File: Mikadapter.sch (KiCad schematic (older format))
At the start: 7 parts, among them J1 RJ45, J2 Conn_01x03_Female, J3 RJ45, J4 Conn_01x03_Female, J5 Conn_01x02_Female, J6 Conn_01x03_Female, J7 Conn_01x02_Female

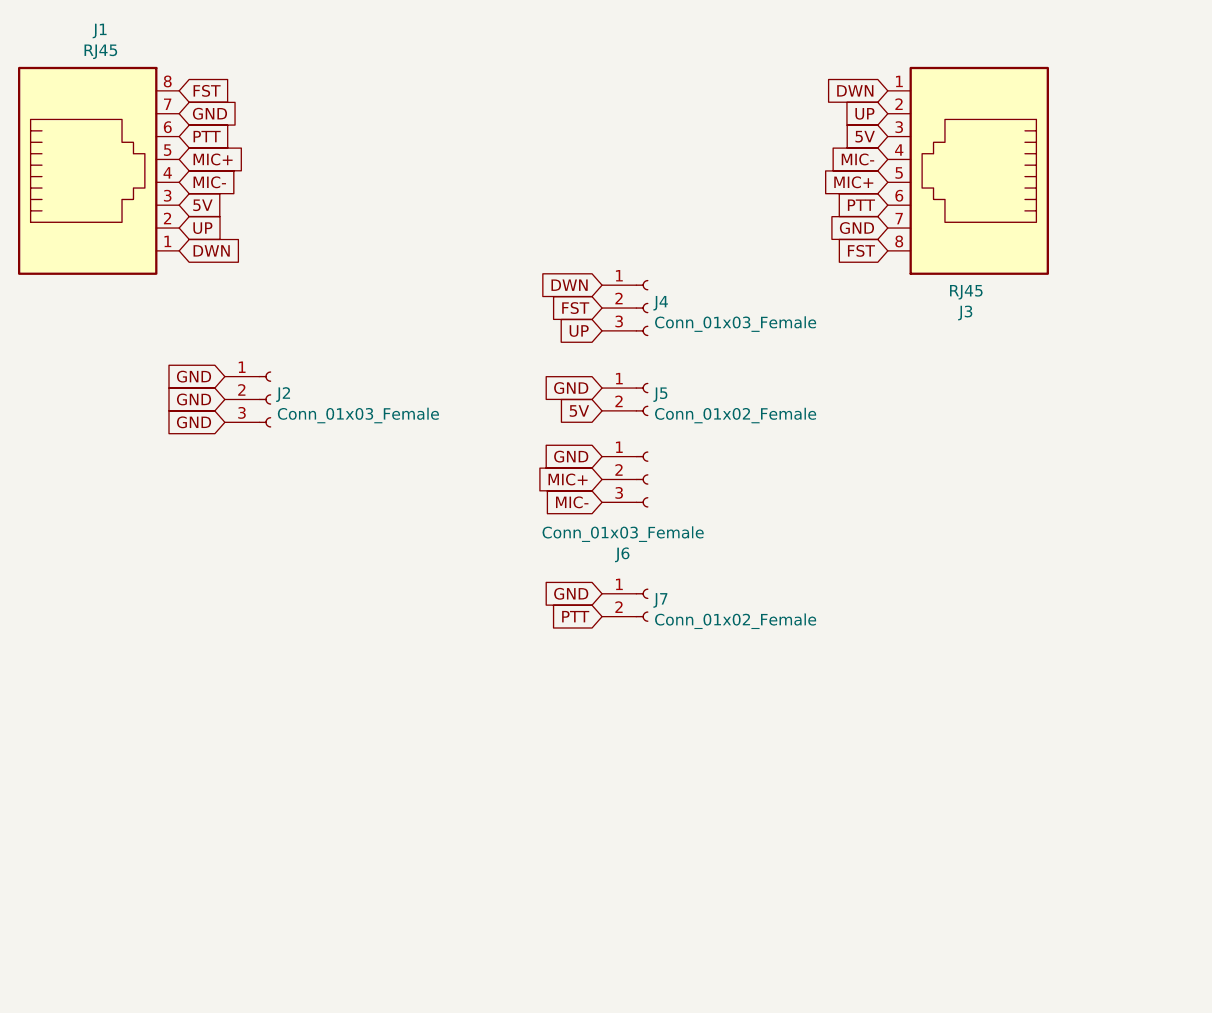
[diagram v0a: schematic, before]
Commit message: changed layout for FST|DWN|UP buttons
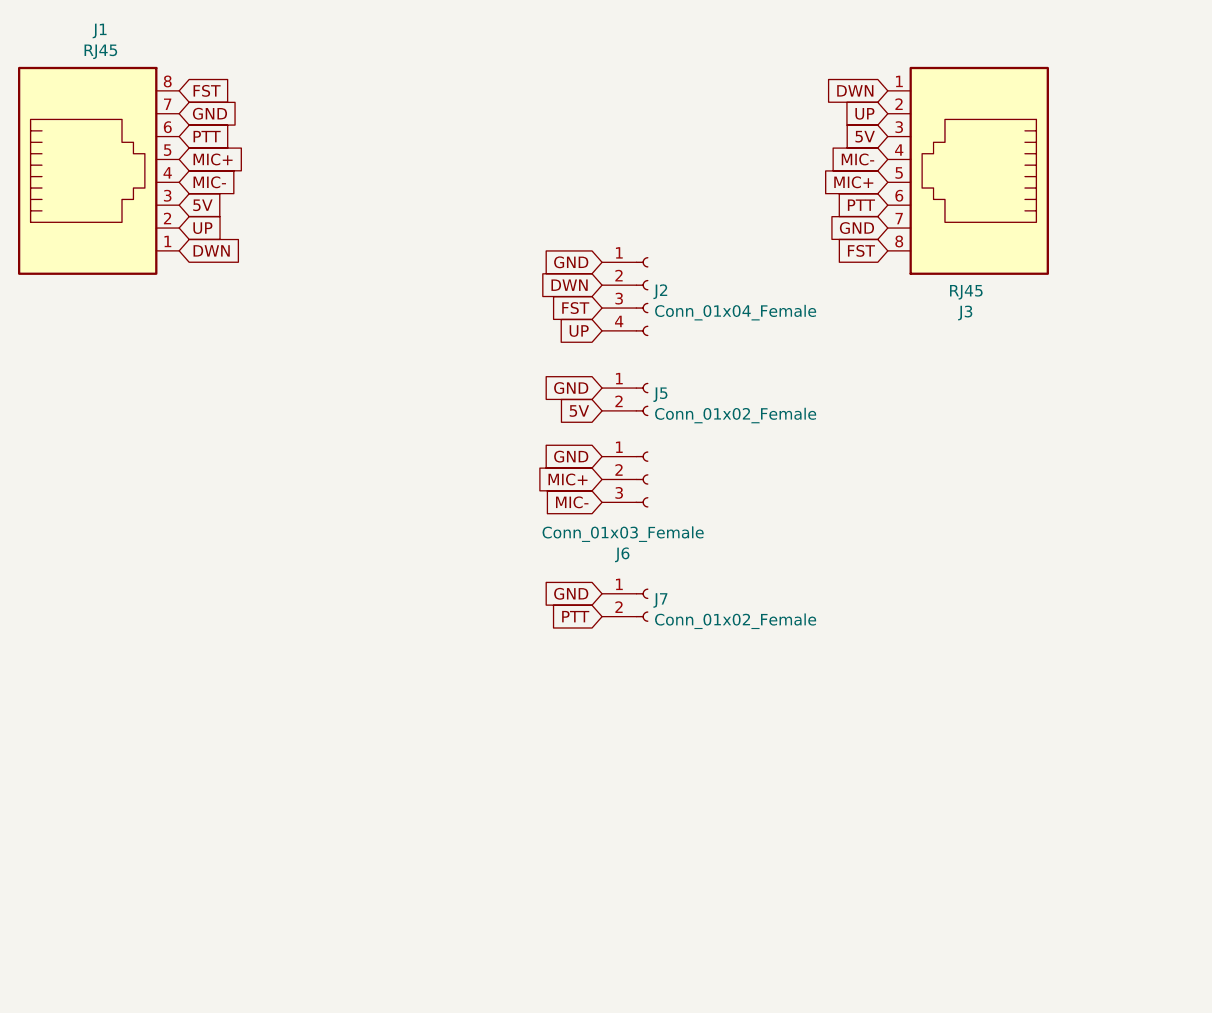
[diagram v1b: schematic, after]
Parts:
- removed J2, J4: Conn_01x03_Female, Connector_PinHeader_2.54mm:PinHeader_1x03_P2.54mm_Vertical, symbol Connector:Conn_01x03_Female
- added J2: Conn_01x04_Female, Connector_PinHeader_2.54mm:PinHeader_1x04_P2.54mm_Vertical, symbol Connector:Conn_01x04_Female
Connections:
- net DWN: now also J2.2 (Pin_2)
- net FST: now also J2.3 (Pin_3)
- net GND: now also J2.1 (Pin_1)
- net UP: now also J2.4 (Pin_4)
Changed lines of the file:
@@
 Text GLabel 5250 3700 0    50   Input ~ 0
 5V
-$Comp
-L Connector:Conn_01x03_Female J4
-U 1 1 607373F2
-P 5450 3250
-F 0 "J4" H 5478 3276 50  0000 L CNN
-F 1 "Conn_01x03_Female" H 5478 3185 50  0000 L CNN
-F 2 "Connector_PinHeader_2.54mm:PinHeader_1x03_P2.54mm_Vertical" H 5450 3250 50  0001 C CNN
-F 3 "~" H 5450 3250 50  0001 C CNN
-	1    5450 3250
-	1    0    0    -1
-$EndComp
-$Comp
-L Connector:Conn_01x03_Female J2
-U 1 1 60738991
-P 3800 3650
-F 0 "J2" H 3828 3676 50  0000 L CNN
-F 1 "Conn_01x03_Female" H 3828 3585 50  0000 L CNN
-F 2 "Connector_PinHeader_2.54mm:PinHeader_1x03_P2.54mm_Vertical" H 3800 3650 50  0001 C CNN
-F 3 "~" H 3800 3650 50  0001 C CNN
-	1    3800 3650
-	1    0    0    -1
-$EndComp
-Text GLabel 3600 3550 0    50   Input ~ 0
-GND
-Text GLabel 3600 3650 0    50   Input ~ 0
-GND
-Text GLabel 3600 3750 0    50   Input ~ 0
+Text GLabel 5250 3050 0    50   Input ~ 0
 GND
 Text GLabel 5250 3150 0    50   Input ~ 0
@@
 Text GLabel 5250 3250 0    50   Input ~ 0
 FST
+$Comp
+L Connector:Conn_01x04_Female J2
+U 1 1 6077AEAE
+P 5450 3150
+F 0 "J2" H 5478 3126 50  0000 L CNN
+F 1 "Conn_01x04_Female" H 5478 3035 50  0000 L CNN
+F 2 "Connector_PinHeader_2.54mm:PinHeader_1x04_P2.54mm_Vertical" H 5450 3150 50  0001 C CNN
+F 3 "~" H 5450 3150 50  0001 C CNN
+	1    5450 3150
+	1    0    0    -1
+$EndComp
 $EndSCHEMATC

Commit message: transformed in KiCAD 6 and changed layout and changed pinout for RJ45
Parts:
- added J1, J3, J4: FC68131, Addtional_DO7GN:CLIFF_FC68131, symbol FC68131:FC68131
- added J9: Conn_01x03_Female, Connector_PinHeader_2.54mm:PinHeader_1x02_P2.54mm_Vertical, symbol Connector:Conn_01x02_Female
- J6: footprint Connector_PinHeader_2.54mm:PinHeader_1x03_P2.54mm_Vertical -> Connector_PinHeader_2.54mm:PinHeader_1x02_P2.54mm_Vertical; symbol Connector:Conn_01x03_Female -> Connector:Conn_01x02_Female
- RJ45OUT1: renamed from J3; value RJ45 -> RJ45OUT
- renumbered J1 to RJ45IN1
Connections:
- net 5V: now also RJ45IN1.6, RJ45OUT1.6; no longer RJ45IN1.3, RJ45OUT1.3
- net DWN: now also RJ45IN1.8, RJ45OUT1.8; no longer RJ45IN1.1, RJ45OUT1.1
- net FST: now also RJ45IN1.1, RJ45OUT1.1; no longer RJ45IN1.8, RJ45OUT1.8
- net GND: now also RJ45IN1.2, RJ45OUT1.2; no longer J6.1 (Pin_1), RJ45IN1.7, RJ45OUT1.7
- net MIC+: now also RJ45IN1.4, RJ45OUT1.4, J1.2; no longer RJ45IN1.5, RJ45OUT1.5
- net MIC-: now also J6.1 (Pin_1), RJ45IN1.5, RJ45OUT1.5, J1.1; no longer J6.3 (Pin_3), RJ45IN1.4, RJ45OUT1.4
- net PTT: now also RJ45IN1.3, RJ45OUT1.3; no longer RJ45IN1.6, RJ45OUT1.6
- net UP: now also RJ45IN1.7, RJ45OUT1.7; no longer RJ45IN1.2, RJ45OUT1.2
- new net Audio+: J3.2, J4.2, J9.2 (Pin_2)
- new net Audio-: J3.1, J4.1, J9.1 (Pin_1)
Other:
- moved on the sheet: RJ45OUT1
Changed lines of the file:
@@
 $EndDescr
 $Comp
-L Connector:RJ45 J1
+L Connector:RJ45 RJ45IN1
 U 1 1 5EAEC084
 P 3000 2700
-F 0 "J1" H 3057 3367 50  0000 C CNN
+F 0 "RJ45IN1" H 3057 3367 50  0000 C CNN
 F 1 "RJ45" H 3057 3276 50  0000 C CNN
 F 2 "Connector_RJ:RJ45_Wuerth_7499010001A_Horizontal" V 3000 2725 50  0001 C CNN
@@
 	1    0    0    -1
 $EndComp
-Text GLabel 3400 3000 2    50   Input ~ 0
-DWN
-Text GLabel 3400 2900 2    50   Input ~ 0
-UP
-Text GLabel 3400 2500 2    50   Input ~ 0
-PTT
-Text GLabel 3400 2300 2    50   Input ~ 0
-FST
-Text GLabel 3400 2400 2    50   Input ~ 0
-GND
-Text GLabel 3400 2600 2    50   Input ~ 0
-MIC+
-Text GLabel 3400 2700 2    50   Input ~ 0
-MIC-
-Text GLabel 3400 2800 2    50   Input ~ 0
-5V
-$Comp
-L Connector:RJ45 J3
+Text GLabel 3950 2700 2    50   Input ~ 0
+UP
+Text GLabel 3950 2300 2    50   Input ~ 0
+PTT
+Text GLabel 3950 2200 2    50   Input ~ 0
+GND
+Text GLabel 3950 2600 2    50   Input ~ 0
+5V
+$Comp
+L Connector:RJ45 RJ45OUT1
 U 1 1 606F46DC
-P 6900 2600
-F 0 "J3" H 6957 3267 50  0000 C CNN
-F 1 "RJ45" H 6957 3176 50  0000 C CNN
-F 2 "Connector_RJ:RJ45_Wuerth_7499010001A_Horizontal" V 6900 2625 50  0001 C CNN
-F 3 "~" V 6900 2625 50  0001 C CNN
-	1    6900 2600
-	-1   0    0    1
-$EndComp
-Text GLabel 6500 2300 0    50   Input ~ 0
-DWN
-Text GLabel 6500 2400 0    50   Input ~ 0
-UP
-Text GLabel 6500 2800 0    50   Input ~ 0
-PTT
-Text GLabel 6500 3000 0    50   Input ~ 0
-FST
-Text GLabel 6500 2900 0    50   Input ~ 0
-GND
-Text GLabel 6500 2700 0    50   Input ~ 0
-MIC+
-Text GLabel 6500 2600 0    50   Input ~ 0
-MIC-
-Text GLabel 6500 2500 0    50   Input ~ 0
-5V
+P 3000 3800
+F 0 "RJ45OUT1" H 3057 4467 50  0000 C CNN
+F 1 "RJ45OUT" H 3057 4376 50  0000 C CNN
+F 2 "Connector_RJ:RJ45_Wuerth_7499010001A_Horizontal" V 3000 3825 50  0001 C CNN
+F 3 "~" V 3000 3825 50  0001 C CNN
+	1    3000 3800
+	1    0    0    -1
+$EndComp
 $Comp
 L Connector:Conn_01x02_Female J7
@@
 Text GLabel 5250 4500 0    50   Input ~ 0
 GND
-$Comp
-L Connector:Conn_01x03_Female J6
-U 1 1 6071E719
-P 5450 4000
-F 0 "J6" H 5342 3675 50  0000 C CNN
-F 1 "Conn_01x03_Female" H 5342 3766 50  0000 C CNN
-F 2 "Connector_PinHeader_2.54mm:PinHeader_1x03_P2.54mm_Vertical" H 5450 4000 50  0001 C CNN
-F 3 "~" H 5450 4000 50  0001 C CNN
-	1    5450 4000
-	1    0    0    -1
-$EndComp
-Text GLabel 5250 4000 0    50   Input ~ 0
-MIC+
-Text GLabel 5250 4100 0    50   Input ~ 0
-MIC-
-Text GLabel 5250 3900 0    50   Input ~ 0
-GND
+Text GLabel 5400 4100 0    50   Input ~ 0
+MIC+
 $Comp
 L Connector:Conn_01x02_Female J5
@@
 	1    0    0    -1
 $EndComp
+Text GLabel 4550 6050 2    50   Input ~ 0
+Audio+
+Text GLabel 6750 5250 0    50   Input ~ 0
+Audio+
+Text GLabel 6750 5150 0    50   Input ~ 0
+Audio-
+$Comp
+L Connector:Conn_01x02_Female J9
+U 1 1 6079AC68
+P 6950 5150
+F 0 "J9" H 6978 5176 50  0000 L CNN
+F 1 "Conn_01x03_Female" H 6978 5085 50  0000 L CNN
+F 2 "Connector_PinHeader_2.54mm:PinHeader_1x02_P2.54mm_Vertical" H 6950 5150 50  0001 C CNN
+F 3 "~" H 6950 5150 50  0001 C CNN
+	1    6950 5150
+	1    0    0    -1
+$EndComp
+$Comp
+L Connector:Conn_01x02_Female J6
+U 1 1 6071E719
+P 5600 4000
+F 0 "J6" H 5492 3675 50  0000 C CNN
+F 1 "Conn_01x03_Female" H 5492 3766 50  0000 C CNN
+F 2 "Connector_PinHeader_2.54mm:PinHeader_1x02_P2.54mm_Vertical" H 5600 4000 50  0001 C CNN
+F 3 "~" H 5600 4000 50  0001 C CNN
+	1    5600 4000
+	1    0    0    -1
+$EndComp
+Text GLabel 3950 2400 2    50   Input ~ 0
+MIC+
+Text GLabel 3950 2100 2    50   Input ~ 0
+FST
+Text GLabel 3950 2800 2    50   Input ~ 0
+DWN
+Text GLabel 5550 6050 2    50   Input ~ 0
+Audio+
+Text GLabel 3650 6100 2    50   Input ~ 0
+MIC+
+Text GLabel 4550 5950 2    50   Input ~ 0
+Audio-
+Text GLabel 5550 5950 2    50   Input ~ 0
+Audio-
+Text GLabel 3650 6000 2    50   Input ~ 0
+MIC-
+Text GLabel 5400 4000 0    50   Input ~ 0
+MIC-
+Text GLabel 3950 2500 2    50   Input ~ 0
+MIC-
+$Comp
+L FC68131:FC68131 J1
+U 1 1 6156A03E
+P 3350 6000
+F 0 "J1" H 3394 6181 50  0000 C CNN
+F 1 "FC68131" H 3394 6090 50  0000 C CNN
+F 2 "Addtional_DO7GN:CLIFF_FC68131" H 3350 6000 50  0001 L BNN
+F 3 "" H 3350 6000 50  0001 L BNN
+F 4 "Manufacturer Recommendations" H 3350 6000 50  0001 L BNN "STANDARD"
+F 5 "Cliff" H 3350 6000 50  0001 L BNN "MANUFACTURER"
+F 6 "6.00 mm" H 3350 6000 50  0001 L BNN "MAXIMUM_PACKAGE_HEIGHT"
+F 7 "5" H 3350 6000 50  0001 L BNN "PARTREV"
+	1    3350 6000
+	1    0    0    -1
+$EndComp
+$Comp
+L FC68131:FC68131 J3
+U 1 1 61571E51
+P 4250 5950
+F 0 "J3" H 4294 6131 50  0000 C CNN
+F 1 "FC68131" H 4294 6040 50  0000 C CNN
+F 2 "Addtional_DO7GN:CLIFF_FC68131" H 4250 5950 50  0001 L BNN
+F 3 "" H 4250 5950 50  0001 L BNN
+F 4 "Manufacturer Recommendations" H 4250 5950 50  0001 L BNN "STANDARD"
+F 5 "Cliff" H 4250 5950 50  0001 L BNN "MANUFACTURER"
+F 6 "6.00 mm" H 4250 5950 50  0001 L BNN "MAXIMUM_PACKAGE_HEIGHT"
+F 7 "5" H 4250 5950 50  0001 L BNN "PARTREV"
+	1    4250 5950
+	1    0    0    -1
+$EndComp
+$Comp
+L FC68131:FC68131 J4
+U 1 1 615753B1
+P 5250 5950
+F 0 "J4" H 5294 6131 50  0000 C CNN
+F 1 "FC68131" H 5294 6040 50  0000 C CNN
+F 2 "Addtional_DO7GN:CLIFF_FC68131" H 5250 5950 50  0001 L BNN
+F 3 "" H 5250 5950 50  0001 L BNN
+F 4 "Manufacturer Recommendations" H 5250 5950 50  0001 L BNN "STANDARD"
+F 5 "Cliff" H 5250 5950 50  0001 L BNN "MANUFACTURER"
+F 6 "6.00 mm" H 5250 5950 50  0001 L BNN "MAXIMUM_PACKAGE_HEIGHT"
+F 7 "5" H 5250 5950 50  0001 L BNN "PARTREV"
+	1    5250 5950
+	1    0    0    -1
+$EndComp
+Text GLabel 3400 3400 2    50   Input ~ 0
+DWN
+Text GLabel 3400 3500 2    50   Input ~ 0
+UP
+Text GLabel 3400 3600 2    50   Input ~ 0
+5V
+Text GLabel 3400 3700 2    50   Input ~ 0
+MIC-
+Text GLabel 3400 3800 2    50   Input ~ 0
+MIC+
+Text GLabel 3400 3900 2    50   Input ~ 0
+PTT
+Text GLabel 3400 4000 2    50   Input ~ 0
+GND
+Text GLabel 3400 4100 2    50   Input ~ 0
+FST
+Text GLabel 3400 2300 2    50   Input ~ 0
+DWN
+Text GLabel 3400 2400 2    50   Input ~ 0
+UP
+Text GLabel 3400 2500 2    50   Input ~ 0
+5V
+Text GLabel 3400 2600 2    50   Input ~ 0
+MIC-
+Text GLabel 3400 2700 2    50   Input ~ 0
+MIC+
+Text GLabel 3400 2800 2    50   Input ~ 0
+PTT
+Text GLabel 3400 2900 2    50   Input ~ 0
+GND
+Text GLabel 3400 3000 2    50   Input ~ 0
+FST
 $EndSCHEMATC
